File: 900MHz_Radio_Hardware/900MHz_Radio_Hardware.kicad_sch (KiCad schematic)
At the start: 10 parts, among them U1 TSR_1-2450

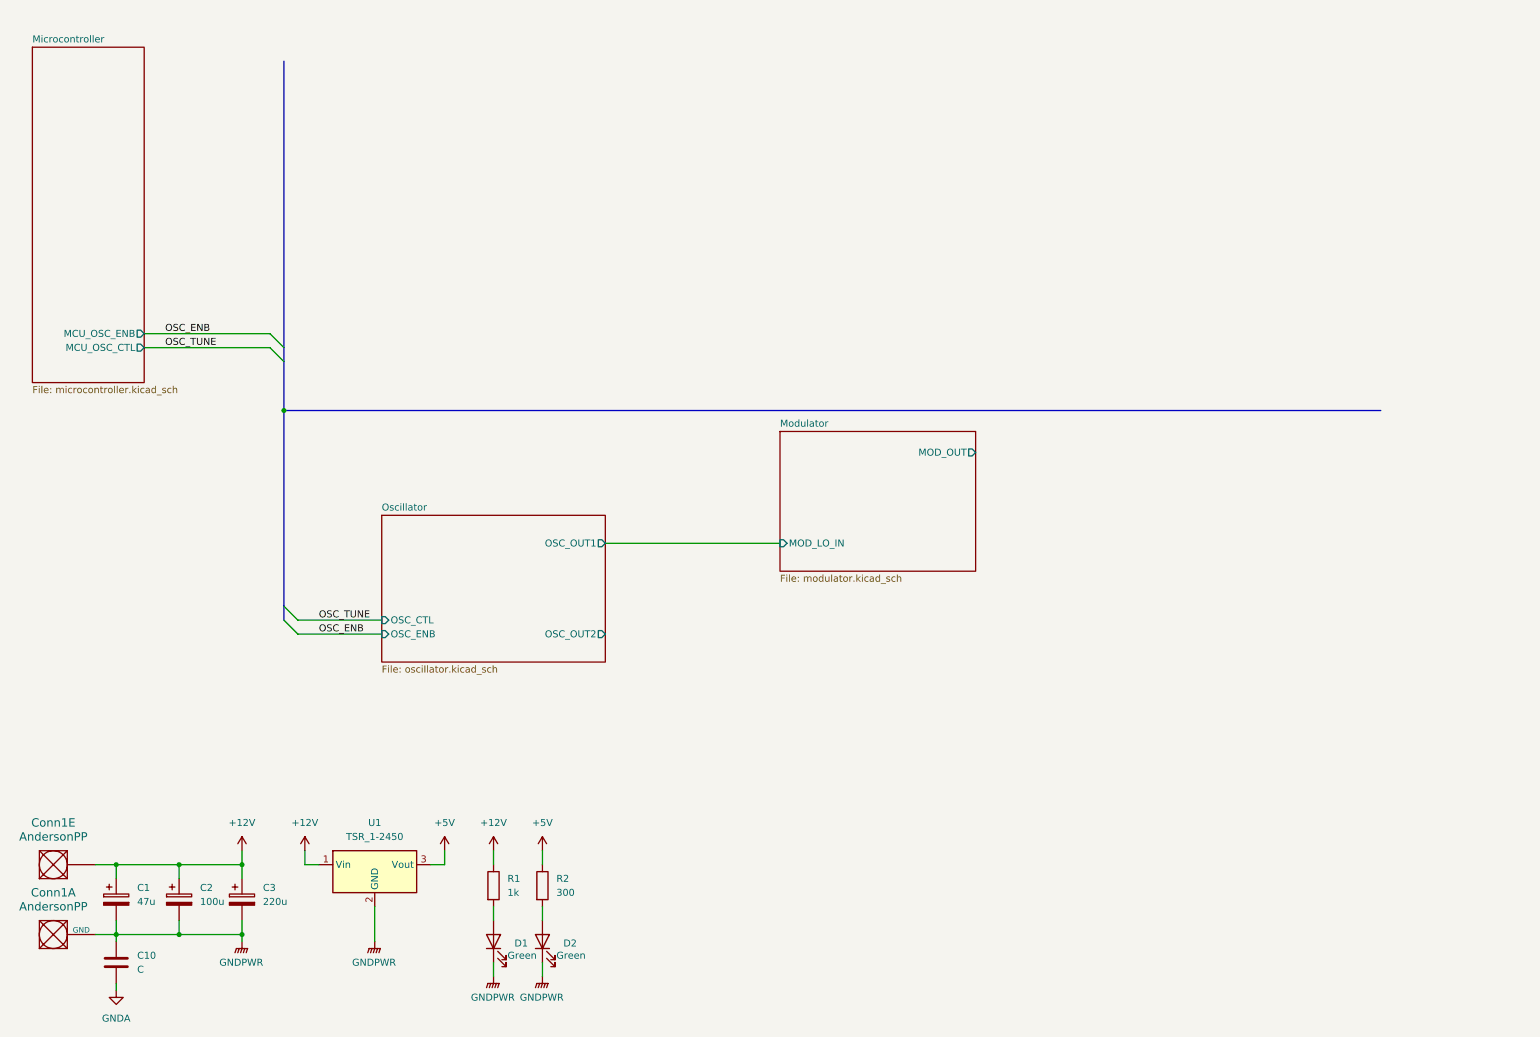
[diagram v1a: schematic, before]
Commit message: Hardware for IQ signal synchronization
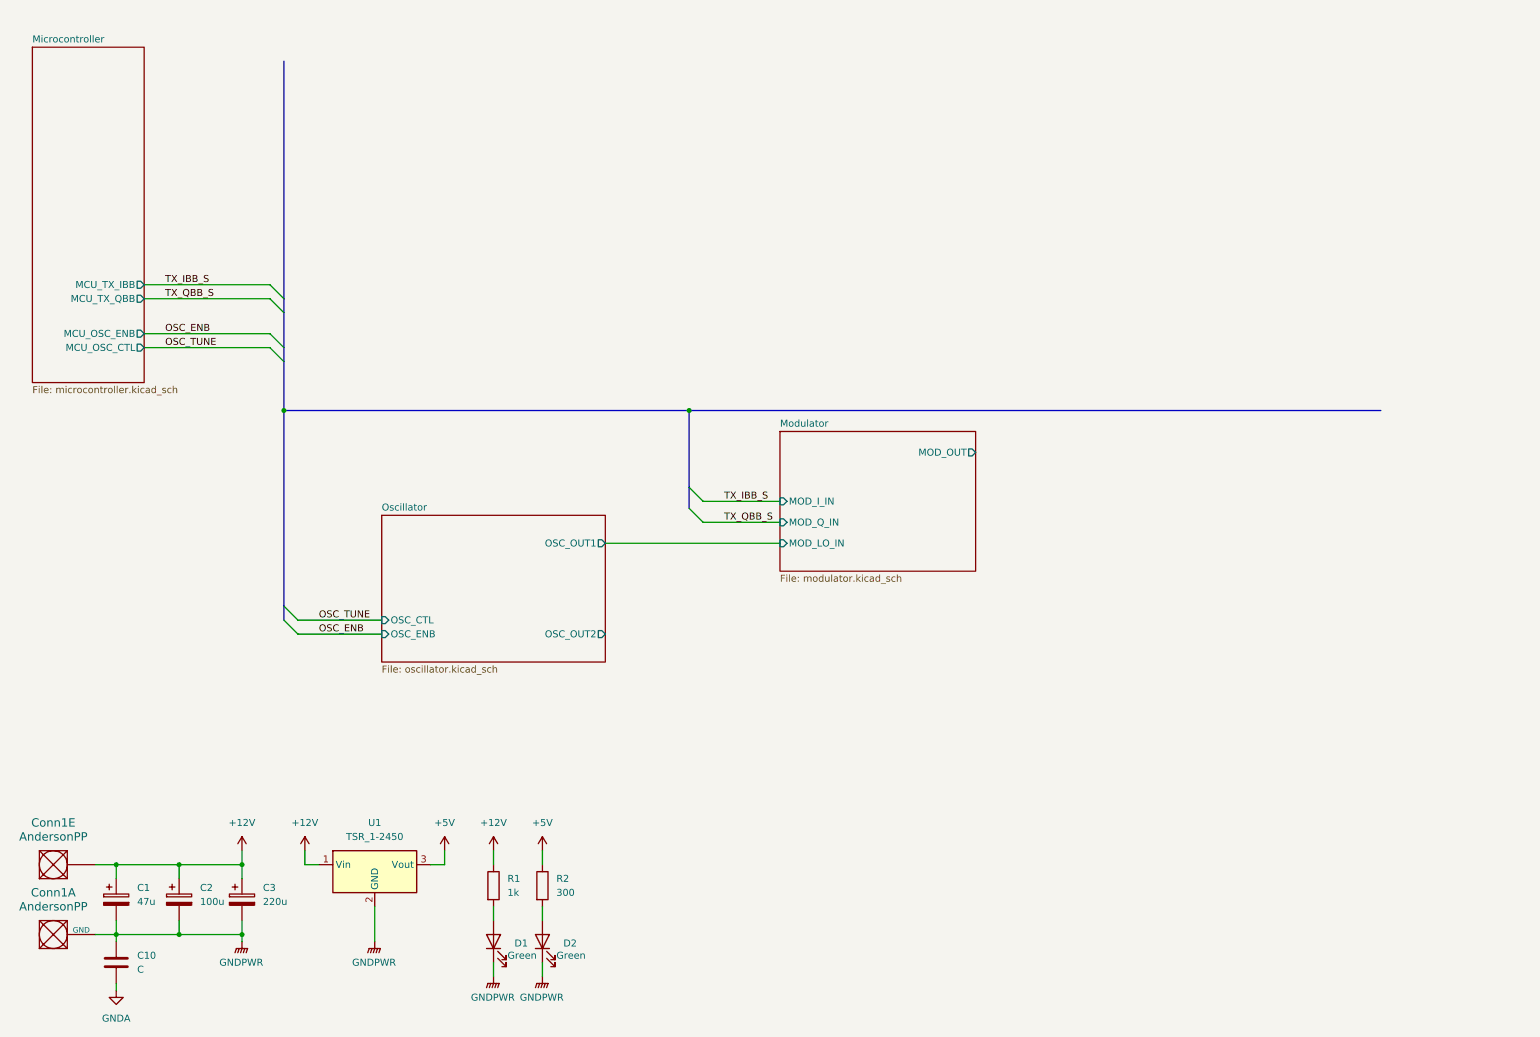
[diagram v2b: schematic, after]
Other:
- sheet Microcontroller ports: added MCU_TX_IBB, MCU_TX_QBB; removed none
- sheet Modulator ports: added MOD_I_IN, MOD_Q_IN; removed none
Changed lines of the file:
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@@
   (junction (at 41.91 167.64) (diameter 0) (color 0 0 0 0)
   )
+  (junction (at 134.62 85.09) (diameter 0) (color 0 0 0 0)
+  )
   (junction (at 53.34 167.64) (diameter 0) (color 0 0 0 0)
   )
@@
   (junction (at 53.34 180.34) (diameter 0) (color 0 0 0 0)
   )
+  (bus_entry (at 134.62 99.06) (size 2.54 2.54)
+    (stroke (width 0) (type default))
+  )
+  (bus_entry (at 58.42 62.23) (size 2.54 2.54)
+    (stroke (width 0) (type default))
+  )
+  (bus_entry (at 58.42 64.77) (size 2.54 2.54)
+    (stroke (width 0) (type default))
+  )
+  (bus_entry (at 134.62 102.87) (size 2.54 2.54)
+    (stroke (width 0) (type default))
+  )
   (bus_entry (at 60.96 120.65) (size 2.54 2.54)
     (stroke (width 0) (type default))
@@
     (stroke (width 0) (type default))
   )
-  (bus (pts (xy 60.96 21.59) (xy 60.96 73.66))
+  (bus (pts (xy 60.96 21.59) (xy 60.96 64.77))
+    (stroke (width 0) (type default))
+  )
+  (wire (pts (xy 35.56 64.77) (xy 58.42 64.77))
+    (stroke (width 0) (type default))
+  )
+  (wire (pts (xy 137.16 105.41) (xy 151.13 105.41))
     (stroke (width 0) (type default))
   )
@@
     (stroke (width 0) (type default))
   )
+  (bus (pts (xy 60.96 64.77) (xy 60.96 67.31))
+    (stroke (width 0) (type default))
+  )
   (wire (pts (xy 53.34 180.34) (xy 53.34 181.61))
     (stroke (width 0) (type default))
@@
     (stroke (width 0) (type default))
   )
-  (bus (pts (xy 60.96 85.09) (xy 260.35 85.09))
+  (bus (pts (xy 60.96 85.09) (xy 134.62 85.09))
     (stroke (width 0) (type default))
   )
@@
     (stroke (width 0) (type default))
   )
+  (bus (pts (xy 134.62 99.06) (xy 134.62 102.87))
+    (stroke (width 0) (type default))
+  )
+  (bus (pts (xy 134.62 85.09) (xy 134.62 99.06))
+    (stroke (width 0) (type default))
+  )
   (bus (pts (xy 60.96 85.09) (xy 60.96 120.65))
     (stroke (width 0) (type default))
@@
     (stroke (width 0) (type default))
   )
+  (bus (pts (xy 134.62 85.09) (xy 260.35 85.09))
+    (stroke (width 0) (type default))
+  )
   (bus (pts (xy 60.96 76.2) (xy 60.96 85.09))
     (stroke (width 0) (type default))
   )
+  (wire (pts (xy 35.56 62.23) (xy 58.42 62.23))
+    (stroke (width 0) (type default))
+  )
   (wire (pts (xy 41.91 180.34) (xy 53.34 180.34))
     (stroke (width 0) (type default))
@@
     (stroke (width 0) (type default))
   )
+  (wire (pts (xy 137.16 101.6) (xy 151.13 101.6))
+    (stroke (width 0) (type default))
+  )
   (wire (pts (xy 26.67 180.34) (xy 30.48 180.34))
     (stroke (width 0) (type default))
   )
+  (bus (pts (xy 60.96 67.31) (xy 60.96 73.66))
+    (stroke (width 0) (type default))
+  )
   (label "OSC_ENB" (at 67.31 125.73 0) (fields_autoplaced)
+    (effects (font (size 1.27 1.27)) (justify left bottom))
+  )
+  (label "TX_QBB_S" (at 140.97 105.41 0) (fields_autoplaced)
+    (effects (font (size 1.27 1.27)) (justify left bottom))
+  )
+  (label "TX_IBB_S" (at 140.97 101.6 0) (fields_autoplaced)
+    (effects (font (size 1.27 1.27)) (justify left bottom))
+  )
+  (label "TX_QBB_S" (at 39.37 64.77 0) (fields_autoplaced)
+    (effects (font (size 1.27 1.27)) (justify left bottom))
+  )
+  (label "TX_IBB_S" (at 39.37 62.23 0) (fields_autoplaced)
     (effects (font (size 1.27 1.27)) (justify left bottom))
   )
@@
       (effects (font (size 1.27 1.27)) (justify right))
     )
+    (pin "MOD_I_IN" input (at 151.13 101.6 180)
+      (effects (font (size 1.27 1.27)) (justify left))
+    )
+    (pin "MOD_Q_IN" input (at 151.13 105.41 180)
+      (effects (font (size 1.27 1.27)) (justify left))
+    )
     (instances
       (project "900MHz_Radio_Hardware"
@@
       (effects (font (size 1.27 1.27)) (justify right))
     )
+    (pin "MCU_TX_IBB" output (at 35.56 62.23 0)
+      (effects (font (size 1.27 1.27)) (justify right))
+    )
+    (pin "MCU_TX_QBB" output (at 35.56 64.77 0)
+      (effects (font (size 1.27 1.27)) (justify right))
+    )

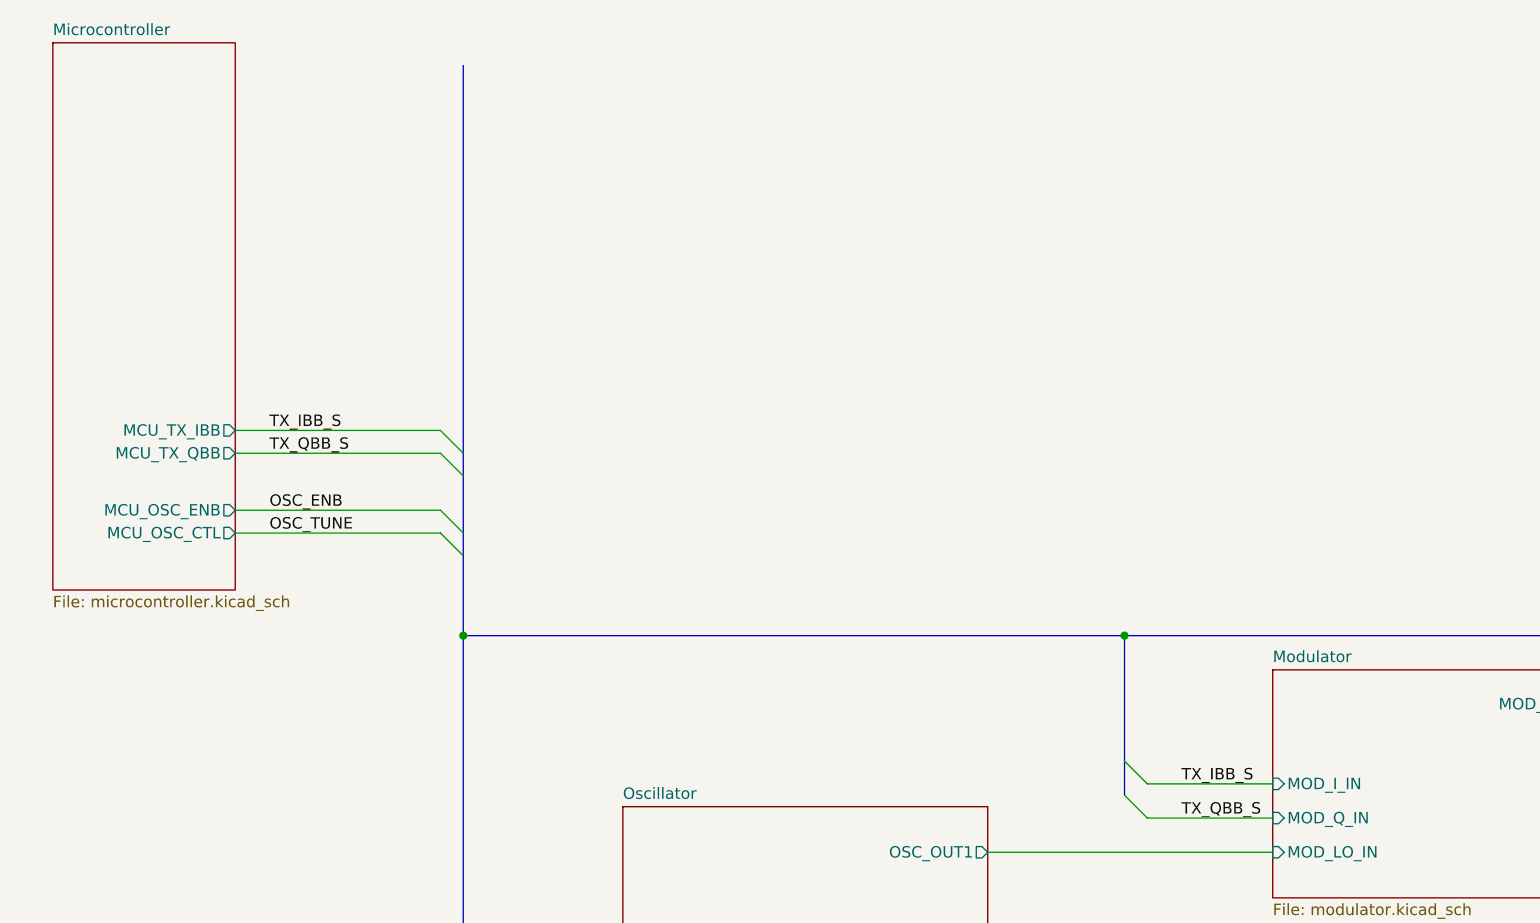
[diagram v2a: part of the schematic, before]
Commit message: Added modulator enable signal
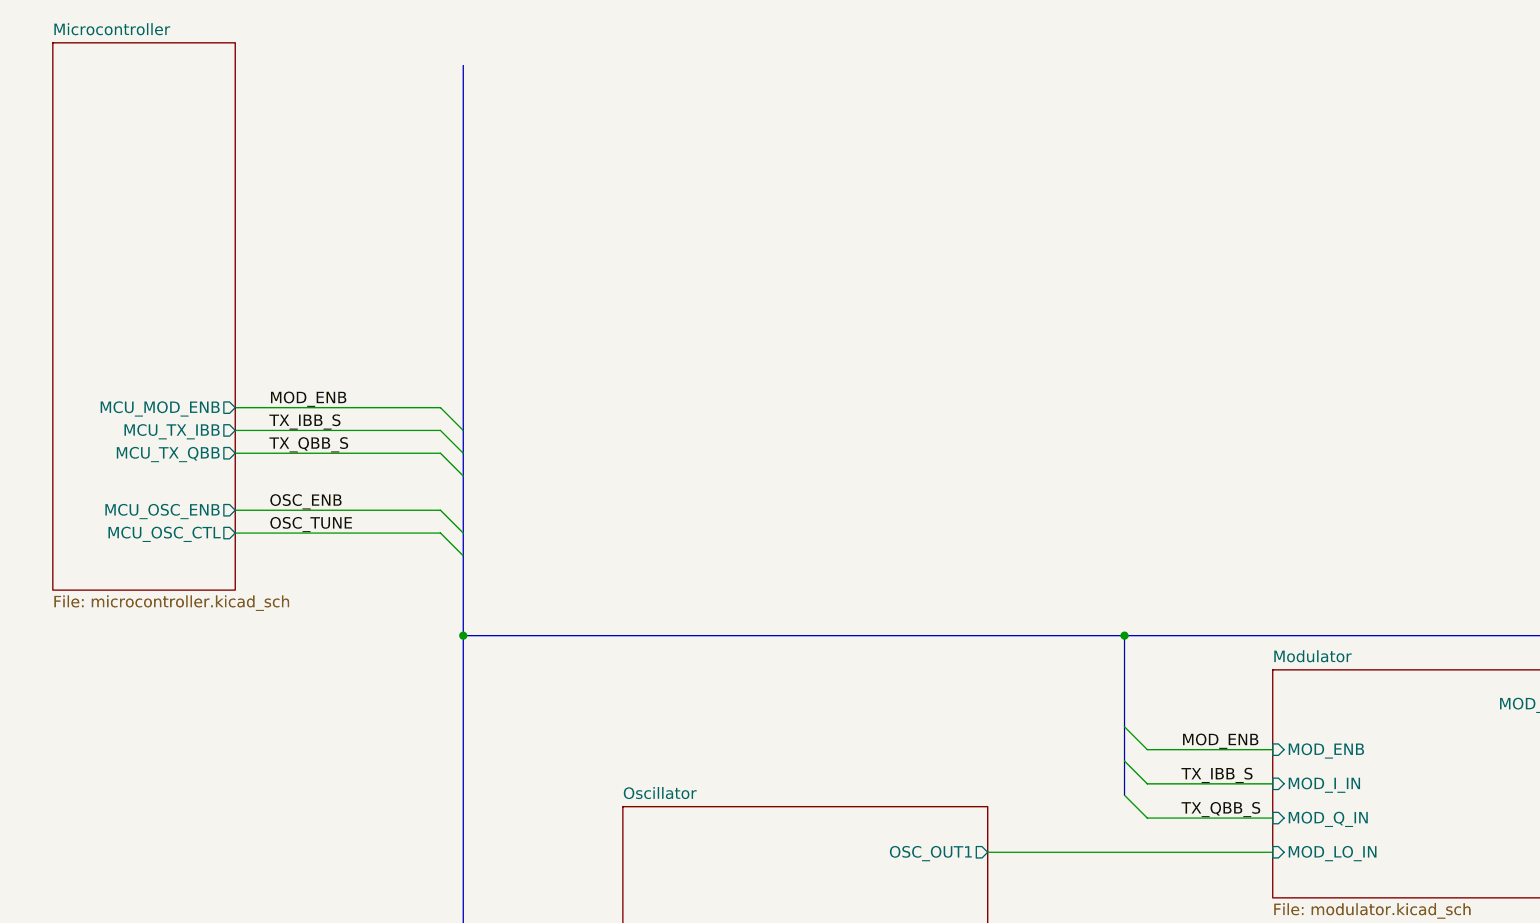
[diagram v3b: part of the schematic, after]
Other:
- sheet Microcontroller ports: added MCU_MOD_ENB; removed none
- sheet Modulator ports: added MOD_ENB; removed none
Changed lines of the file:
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@@
+    (stroke (width 0) (type default))
+  )
+  (bus_entry (at 134.62 95.25) (size 2.54 2.54)
     (stroke (width 0) (type default))
   )
@@
     (stroke (width 0) (type default))
   )
+  (bus_entry (at 58.42 59.69) (size 2.54 2.54)
+    (stroke (width 0) (type default))
+  )
   (wire (pts (xy 26.67 167.64) (xy 30.48 167.64))
     (stroke (width 0) (type default))
   )
+  (wire (pts (xy 137.16 97.79) (xy 151.13 97.79))
+    (stroke (width 0) (type default))
+  )
   (wire (pts (xy 99.06 185.42) (xy 99.06 187.96))
     (stroke (width 0) (type default))
@@
     (stroke (width 0) (type default))
   )
-  (bus (pts (xy 60.96 21.59) (xy 60.96 64.77))
+  (bus (pts (xy 60.96 21.59) (xy 60.96 62.23))
     (stroke (width 0) (type default))
   )
@@
     (stroke (width 0) (type default))
   )
+  (bus (pts (xy 60.96 62.23) (xy 60.96 64.77))
+    (stroke (width 0) (type default))
+  )
   (bus (pts (xy 60.96 73.66) (xy 60.96 76.2))
     (stroke (width 0) (type default))
@@
     (stroke (width 0) (type default))
   )
+  (wire (pts (xy 35.56 59.69) (xy 58.42 59.69))
+    (stroke (width 0) (type default))
+  )
   (bus (pts (xy 60.96 85.09) (xy 134.62 85.09))
     (stroke (width 0) (type default))
@@
     (stroke (width 0) (type default))
   )
-  (bus (pts (xy 134.62 85.09) (xy 134.62 99.06))
+  (bus (pts (xy 134.62 85.09) (xy 134.62 95.25))
     (stroke (width 0) (type default))
   )
@@
     (stroke (width 0) (type default))
   )
+  (bus (pts (xy 134.62 95.25) (xy 134.62 99.06))
+    (stroke (width 0) (type default))
+  )
   (wire (pts (xy 35.56 73.66) (xy 58.42 73.66))
     (stroke (width 0) (type default))
@@
     (stroke (width 0) (type default))
   )
+  (label "MOD_ENB" (at 39.37 59.69 0) (fields_autoplaced)
+    (effects (font (size 1.27 1.27)) (justify left bottom))
+  )
   (label "OSC_ENB" (at 67.31 125.73 0) (fields_autoplaced)
     (effects (font (size 1.27 1.27)) (justify left bottom))
@@
   )
   (label "OSC_TUNE" (at 39.37 73.66 0) (fields_autoplaced)
+    (effects (font (size 1.27 1.27)) (justify left bottom))
+  )
+  (label "MOD_ENB" (at 140.97 97.79 0) (fields_autoplaced)
     (effects (font (size 1.27 1.27)) (justify left bottom))
   )
@@
       (effects (font (size 1.27 1.27)) (justify left))
     )
+    (pin "MOD_ENB" input (at 151.13 97.79 180)
+      (effects (font (size 1.27 1.27)) (justify left))
+    )
     (instances
       (project "900MHz_Radio_Hardware"
@@
       (effects (font (size 1.27 1.27)) (justify right))
     )
+    (pin "MCU_MOD_ENB" output (at 35.56 59.69 0)
+      (effects (font (size 1.27 1.27)) (justify right))
+    )
